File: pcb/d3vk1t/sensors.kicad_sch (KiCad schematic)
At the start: 0 parts

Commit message: [doc: update mcu pinout, pcb: update board shape]
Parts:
- added IC1: LSM6DSMTR, PQFN50P300X250X86-14N, symbol db-sensor-imu:LSM6DSMTR
- added IC2: HDC1080DMBR, SON100P300X300X80-7N, symbol db-sensor-temp:HDC1080DMBR
- added IC3: LPS22HBTR, PQFN50P200X200X80-10N, symbol db-sensor-baro:LPS22HBTR
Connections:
- new net: IC1.6 (GND), IC1.7 (GND)
- new net: IC3.8 (GND), IC3.9 (GND)
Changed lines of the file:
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@@
 (kicad_sch (version 20230121) (generator eeschema)
   (paper "A4")
+  (symbol (lib_id "db-sensor-imu:LSM6DSMTR") (at 78.486 66.294 0) (unit 1)
+    (in_bom yes) (on_board yes) (dnp no) (fields_autoplaced)
+    (property "Reference" "IC1" (at 78.486 46.736 0)
+      (effects (font (size 1.27 1.27)))
+    )
+    (property "Value" "LSM6DSMTR" (at 78.486 49.276 0)
+      (effects (font (size 1.27 1.27)))
+    )
+    (property "Footprint" "PQFN50P300X250X86-14N" (at 78.486 66.294 0)
+      (effects (font (size 1.27 1.27)) (justify bottom) hide)
+    )
+    (property "Datasheet" "" (at 78.486 66.294 0)
+      (effects (font (size 1.27 1.27)) hide)
+    )
+    (property "MANUFACTURER" "STMicroelectronics" (at 78.486 66.294 0)
+      (effects (font (size 1.27 1.27)) (justify bottom) hide)
+    )
+    (property "PARTREV" "Rev 7" (at 78.486 66.294 0)
+      (effects (font (size 1.27 1.27)) (justify bottom) hide)
+    )
+    (property "STANDARD" "IPC 7351B" (at 78.486 66.294 0)
+      (effects (font (size 1.27 1.27)) (justify bottom) hide)
+    )
+    (property "MAXIMUM_PACKAGE_HEIGHT" "0.86 mm" (at 78.486 66.294 0)
+      (effects (font (size 1.27 1.27)) (justify bottom) hide)
+    )
+    (pin "1")
+    (pin "10")
+    (pin "11")
+    (pin "12")
+    (pin "13")
+    (pin "14")
+    (pin "2")
+    (pin "3")
+    (pin "4")
+    (pin "5")
+    (pin "6")
+    (pin "7")
+    (pin "8")
+    (pin "9")
+    (instances
+      (project "d3vk1t"
+        (path "/4ea523ae-7c45-478e-a9cc-6f4833d1a9d5/e38a53da-cd3b-4abc-bf47-dbcc2772d10e"
+          (reference "IC1") (unit 1)
+        )
+      )
+    )
+  )
+  (symbol (lib_id "db-sensor-baro:LPS22HBTR") (at 194.056 120.142 0) (unit 1)
+    (in_bom yes) (on_board yes) (dnp no) (fields_autoplaced)
+    (property "Reference" "IC3" (at 194.056 98.044 0)
+      (effects (font (size 1.27 1.27)))
+    )
+    (property "Value" "LPS22HBTR" (at 194.056 100.584 0)
+      (effects (font (size 1.27 1.27)))
+    )
+    (property "Footprint" "PQFN50P200X200X80-10N" (at 194.056 120.142 0)
+      (effects (font (size 1.27 1.27)) (justify bottom) hide)
+    )
+    (property "Datasheet" "" (at 194.056 120.142 0)
+      (effects (font (size 1.27 1.27)) hide)
+    )
+    (property "MANUFACTURER" "STMicroelectronics" (at 194.056 120.142 0)
+      (effects (font (size 1.27 1.27)) (justify bottom) hide)
+    )
+    (property "PARTREV" "6" (at 194.056 120.142 0)
+      (effects (font (size 1.27 1.27)) (justify bottom) hide)
+    )
+    (property "STANDARD" "IPC-7351B" (at 194.056 120.142 0)
+      (effects (font (size 1.27 1.27)) (justify bottom) hide)
+    )
+    (property "MAXIMUM_PACKAGE_HEIGHT" "0.8mm" (at 194.056 120.142 0)
+      (effects (font (size 1.27 1.27)) (justify bottom) hide)
+    )
+    (pin "1")
+    (pin "10")
+    (pin "2")
+    (pin "3")
+    (pin "4")
+    (pin "5")
+    (pin "6")
+    (pin "7")
+    (pin "8")
+    (pin "9")
+    (instances
+      (project "d3vk1t"
+        (path "/4ea523ae-7c45-478e-a9cc-6f4833d1a9d5/e38a53da-cd3b-4abc-bf47-dbcc2772d10e"
+          (reference "IC3") (unit 1)
+        )
+      )
+    )
+  )
+  (symbol (lib_id "db-sensor-temp:HDC1080DMBR") (at 195.834 66.548 0) (unit 1)
+    (in_bom yes) (on_board yes) (dnp no) (fields_autoplaced)
+    (property "Reference" "IC2" (at 195.834 50.038 0)
+      (effects (font (size 1.27 1.27)))
+    )
+    (property "Value" "HDC1080DMBR" (at 195.834 52.578 0)
+      (effects (font (size 1.27 1.27)))
+    )
+    (property "Footprint" "SON100P300X300X80-7N" (at 195.834 66.548 0)
+      (effects (font (size 1.27 1.27)) (justify bottom) hide)
+    )
+    (property "Datasheet" "" (at 195.834 66.548 0)
+      (effects (font (size 1.27 1.27)) hide)
+    )
+    (property "MANUFACTURER" "Texas Instruments" (at 195.834 66.548 0)
+      (effects (font (size 1.27 1.27)) (justify bottom) hide)
+    )
+    (property "MAXIMUM_PACKAGE_HEIGHT" "0.8 mm" (at 195.834 66.548 0)
+      (effects (font (size 1.27 1.27)) (justify bottom) hide)
+    )
+    (property "STANDARD" "Manufacturer Recommendations" (at 195.834 66.548 0)
+      (effects (font (size 1.27 1.27)) (justify bottom) hide)
+    )
+    (property "PARTREV" "A" (at 195.834 66.548 0)
+      (effects (font (size 1.27 1.27)) (justify bottom) hide)
+    )
+    (pin "1")
+    (pin "2")
+    (pin "3")
+    (pin "4")
+    (pin "5")
+    (pin "6")
+    (pin "7")
+    (instances
+      (project "d3vk1t"
+        (path "/4ea523ae-7c45-478e-a9cc-6f4833d1a9d5/e38a53da-cd3b-4abc-bf47-dbcc2772d10e"
+          (reference "IC2") (unit 1)
+        )
+      )
+    )
+  )
 )

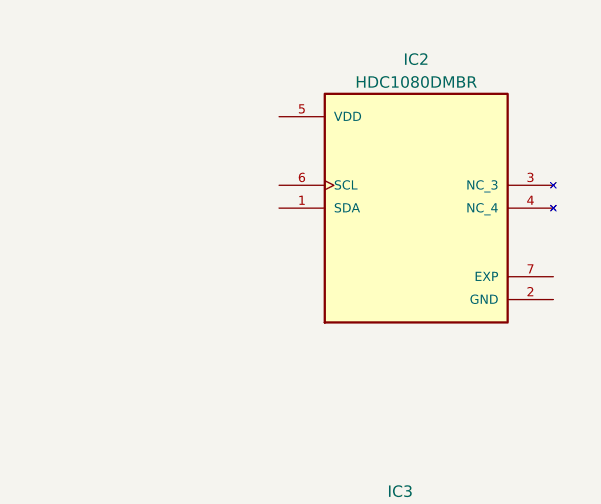
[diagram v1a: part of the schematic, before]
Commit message: doc: added f4 hw dev doc
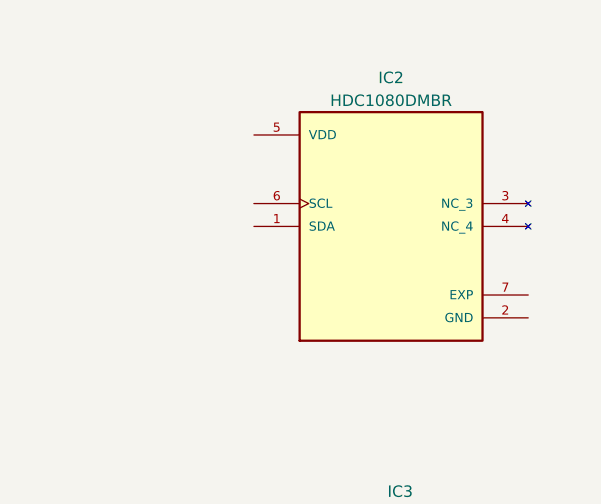
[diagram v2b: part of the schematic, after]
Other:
- moved on the sheet: IC2
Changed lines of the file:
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@@
     )
   )
-  (symbol (lib_id "db-sensor-temp:HDC1080DMBR") (at 195.834 66.548 0) (unit 1)
+  (symbol (lib_id "db-sensor-temp:HDC1080DMBR") (at 193.04 68.58 0) (unit 1)
     (in_bom yes) (on_board yes) (dnp no) (fields_autoplaced)
-    (property "Reference" "IC2" (at 195.834 50.038 0)
+    (property "Reference" "IC2" (at 193.04 52.07 0)
       (effects (font (size 1.27 1.27)))
     )
-    (property "Value" "HDC1080DMBR" (at 195.834 52.578 0)
+    (property "Value" "HDC1080DMBR" (at 193.04 54.61 0)
       (effects (font (size 1.27 1.27)))
     )
-    (property "Footprint" "SON100P300X300X80-7N" (at 195.834 66.548 0)
+    (property "Footprint" "SON100P300X300X80-7N" (at 193.04 68.58 0)
       (effects (font (size 1.27 1.27)) (justify bottom) hide)
     )
-    (property "Datasheet" "" (at 195.834 66.548 0)
+    (property "Datasheet" "" (at 193.04 68.58 0)
       (effects (font (size 1.27 1.27)) hide)
     )
-    (property "MANUFACTURER" "Texas Instruments" (at 195.834 66.548 0)
+    (property "MANUFACTURER" "Texas Instruments" (at 193.04 68.58 0)
       (effects (font (size 1.27 1.27)) (justify bottom) hide)
     )
-    (property "MAXIMUM_PACKAGE_HEIGHT" "0.8 mm" (at 195.834 66.548 0)
+    (property "MAXIMUM_PACKAGE_HEIGHT" "0.8 mm" (at 193.04 68.58 0)
       (effects (font (size 1.27 1.27)) (justify bottom) hide)
     )
-    (property "STANDARD" "Manufacturer Recommendations" (at 195.834 66.548 0)
+    (property "STANDARD" "Manufacturer Recommendations" (at 193.04 68.58 0)
       (effects (font (size 1.27 1.27)) (justify bottom) hide)
     )
-    (property "PARTREV" "A" (at 195.834 66.548 0)
+    (property "PARTREV" "A" (at 193.04 68.58 0)
       (effects (font (size 1.27 1.27)) (justify bottom) hide)
     )

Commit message: [update all schematics sheets]
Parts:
- added C1 (x2), C2 (x3): 100nF, Capacitor_SMD:C_0402_1005Metric, symbol Device:C_Small
- added R5 (x4): 10K, Resistor_SMD:R_0402_1005Metric, symbol Device:R_Small
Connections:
- net SPI1_MISO: now reaches IC1.1 (SDO/SA0)
- net SPI1_MISO: now also IC3.5 (SDO/SA0)
- net ACC_CS: now reaches IC1.12 (CS)
- net ACC_CS: now also R5.1
- net SPI1_CLK: now reaches IC1.13 (SCL/SPC)
- net SPI1_CLK: now also IC3.2 (SCL/SPC)
- net SPI1_MOSI: now reaches IC1.14 (SDA/SDI/SDO)
- net SPI1_MOSI: now also IC3.4 (SDA/SDI/SDO)
- net GND: now reaches IC1.2 (SDX)
- net GND: now also IC1.3 (SCX), IC1.6 (GND), IC1.7 (GND), IC2.2 (GND), IC2.7 (EXP), IC3.3 (RESERVED), IC3.8 (GND), IC3.9 (GND), C1.2, C1.2, C2.2, C2.2, C2.2
- net ACC_INT: now reaches IC1.4 (INT1)
- net +3.3V: now reaches IC1.5 (VDDIO)
- net +3.3V: now also IC1.8 (VDD), IC2.5 (VDD), IC3.1 (VDD_IO), IC3.10 (VDD), C1.1, C1.1, C2.1, C2.1, C2.1, R5.2, R5.2, R5.2, R5.2
- net BARO_CS: now reaches IC3.6 (CS)
- net BARO_CS: now also R5.1
- net I2C1_SDA: now reaches IC2.1 (SDA)
- net I2C1_SDA: now also R5.1
- net I2C1_SCL: now reaches IC2.6 (SCL)
- net I2C1_SCL: now also R5.1
- no-connect marks 0 -> 4
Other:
- moved on the sheet: IC2, IC3

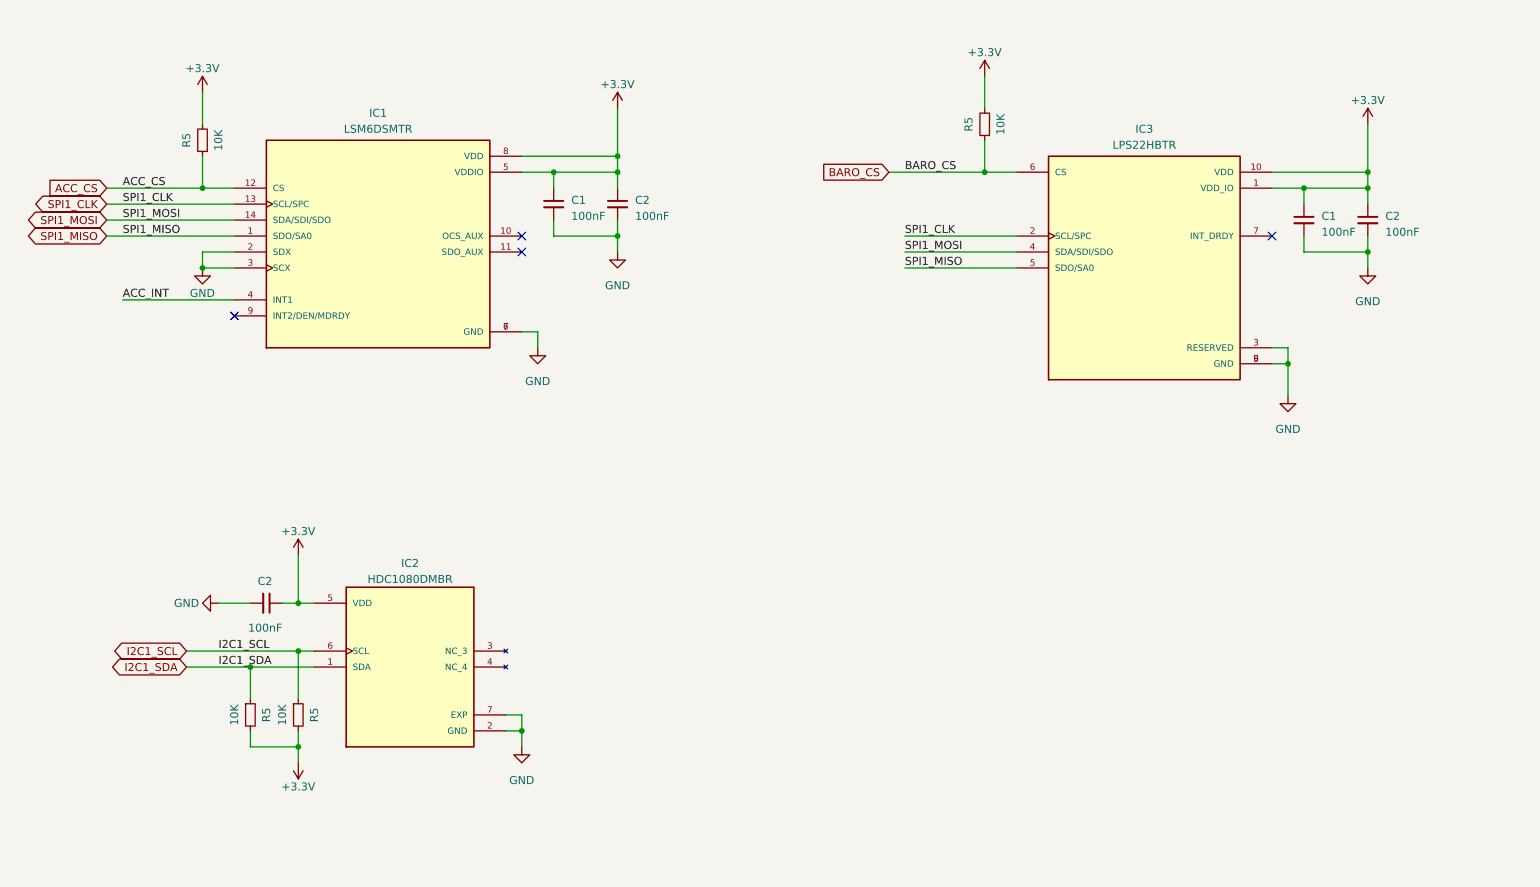
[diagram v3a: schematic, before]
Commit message: sch: update all sch sheets.
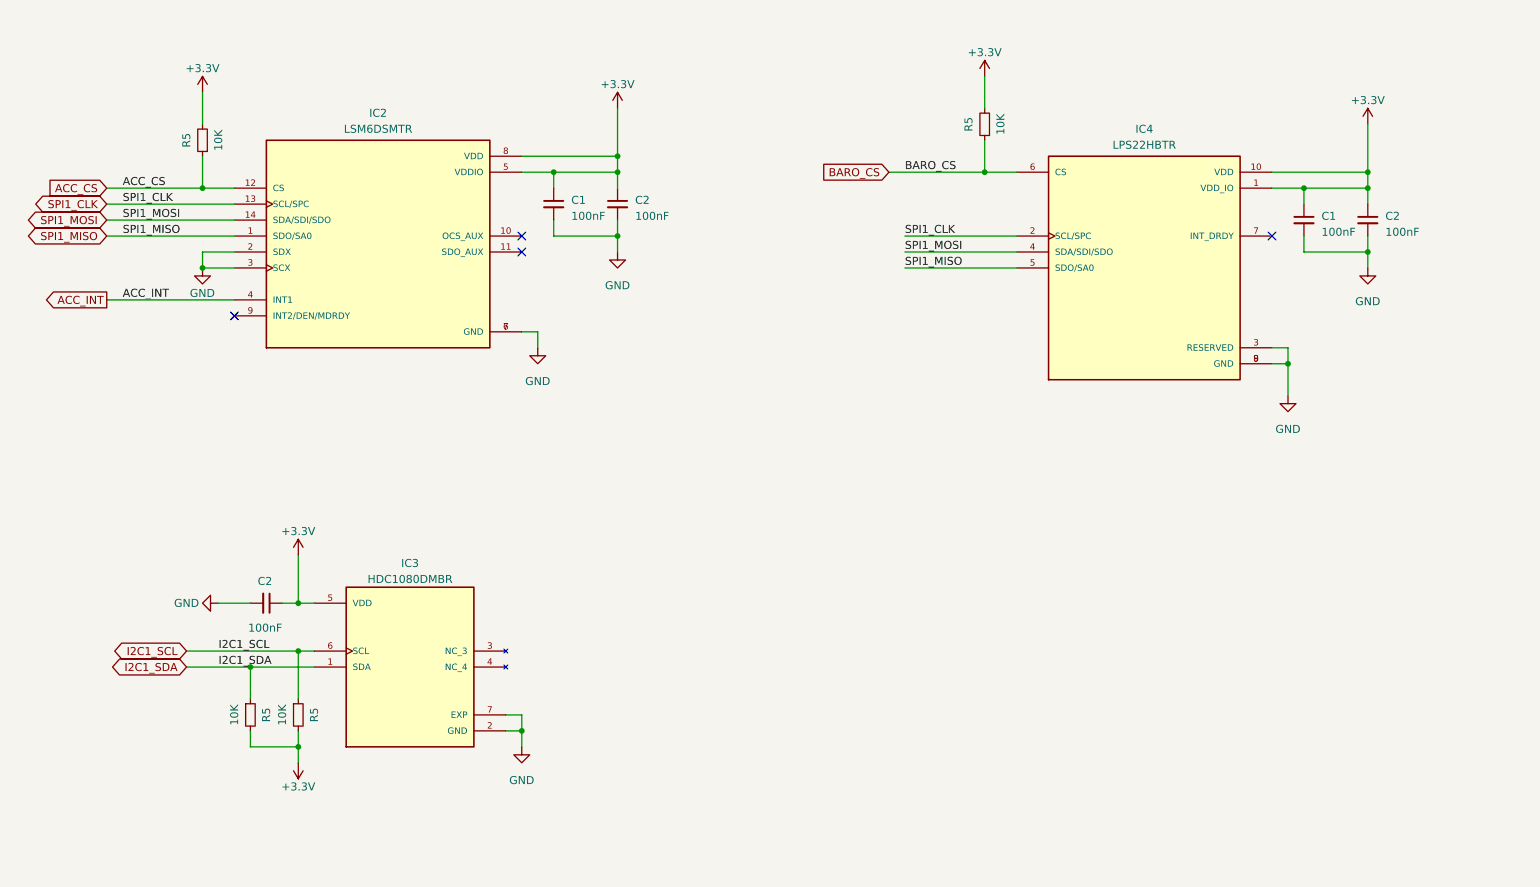
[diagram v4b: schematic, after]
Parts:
- IC2: renamed from IC1; footprint PQFN50P300X250X86-14N -> db:PQFN50P300X250X86-14N
- IC3: renamed from IC2; footprint SON100P300X300X80-7N -> db:SON100P300X300X80-7N
- IC4: renamed from IC3; footprint PQFN50P200X200X80-10N -> db:PQFN50P200X200X80-10N
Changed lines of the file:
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@@
     (stroke (width 0) (type default))
   )
-  (wire (pts (xy 38.1 76.2) (xy 55.88 76.2))
+  (wire (pts (xy 35.56 76.2) (xy 55.88 76.2))
     (stroke (width 0) (type default))
   )
@@
     )
   )
+  (global_label "ACC_INT" (shape output) (at 35.56 76.2 180) (fields_autoplaced)
+    (effects (font (size 1.27 1.27)) (justify right))
+    (property "Intersheetrefs" "${INTERSHEET_REFS}" (at 25.1551 76.2 0)
+      (effects (font (size 1.27 1.27)) (justify right) hide)
+    )
+  )
   (symbol (lib_id "db-sensor-imu:LSM6DSMTR") (at 78.74 66.04 0) (unit 1)
     (in_bom yes) (on_board yes) (dnp no) (fields_autoplaced)
-    (property "Reference" "IC1" (at 78.74 46.482 0)
+    (property "Reference" "IC2" (at 78.74 46.482 0)
       (effects (font (size 1.27 1.27)))
     )
@@
       (effects (font (size 1.27 1.27)))
     )
-    (property "Footprint" "PQFN50P300X250X86-14N" (at 78.74 66.04 0)
+    (property "Footprint" "db:PQFN50P300X250X86-14N" (at 78.74 66.04 0)
       (effects (font (size 1.27 1.27)) (justify bottom) hide)
     )
@@
       (project "d3vk1t"
         (path "/4ea523ae-7c45-478e-a9cc-6f4833d1a9d5/e38a53da-cd3b-4abc-bf47-dbcc2772d10e"
-          (reference "IC1") (unit 1)
+          (reference "IC2") (unit 1)
         )
       )
@@
   (symbol (lib_id "db-sensor-baro:LPS22HBTR") (at 200.66 71.12 0) (unit 1)
     (in_bom yes) (on_board yes) (dnp no) (fields_autoplaced)
-    (property "Reference" "IC3" (at 200.66 49.022 0)
+    (property "Reference" "IC4" (at 200.66 49.022 0)
       (effects (font (size 1.27 1.27)))
     )
@@
       (effects (font (size 1.27 1.27)))
     )
-    (property "Footprint" "PQFN50P200X200X80-10N" (at 200.66 71.12 0)
+    (property "Footprint" "db:PQFN50P200X200X80-10N" (at 200.66 71.12 0)
       (effects (font (size 1.27 1.27)) (justify bottom) hide)
     )
@@
       (project "d3vk1t"
         (path "/4ea523ae-7c45-478e-a9cc-6f4833d1a9d5/e38a53da-cd3b-4abc-bf47-dbcc2772d10e"
-          (reference "IC3") (unit 1)
+          (reference "IC4") (unit 1)
         )
       )
@@
   (symbol (lib_id "db-sensor-temp:HDC1080DMBR") (at 83.82 134.62 0) (unit 1)
     (in_bom yes) (on_board yes) (dnp no) (fields_autoplaced)
-    (property "Reference" "IC2" (at 83.82 118.11 0)
+    (property "Reference" "IC3" (at 83.82 118.11 0)
       (effects (font (size 1.27 1.27)))
     )
@@
       (effects (font (size 1.27 1.27)))
     )
-    (property "Footprint" "SON100P300X300X80-7N" (at 83.82 134.62 0)
+    (property "Footprint" "db:SON100P300X300X80-7N" (at 83.82 134.62 0)
       (effects (font (size 1.27 1.27)) (justify bottom) hide)
     )
@@
       (project "d3vk1t"
         (path "/4ea523ae-7c45-478e-a9cc-6f4833d1a9d5/e38a53da-cd3b-4abc-bf47-dbcc2772d10e"
-          (reference "IC2") (unit 1)
-        )
-      )
+          (reference "IC3") (unit 1)
+        )
+      )

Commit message: project update  - update pcb layout.  - update schmatics sheets.  - added manufacturing files.  - added documentation files.
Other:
- note added: "IMU SENSOR"
- note added: "PRESSURE SENSOR"
- note added: "TEMPERATURE & HUMIDITY SENSOR"
- title: (none) -> Sensors
- moved on the sheet: C1, C2, IC2, IC3, IC4, R5
